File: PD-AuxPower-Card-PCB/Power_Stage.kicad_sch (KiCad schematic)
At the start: 33 parts, among them J4 2.54mm terminal, Q1 FDMC86520L, T1 EFD10, U8 EL3H7(C)(TA)-G, U9 TL431DBZ

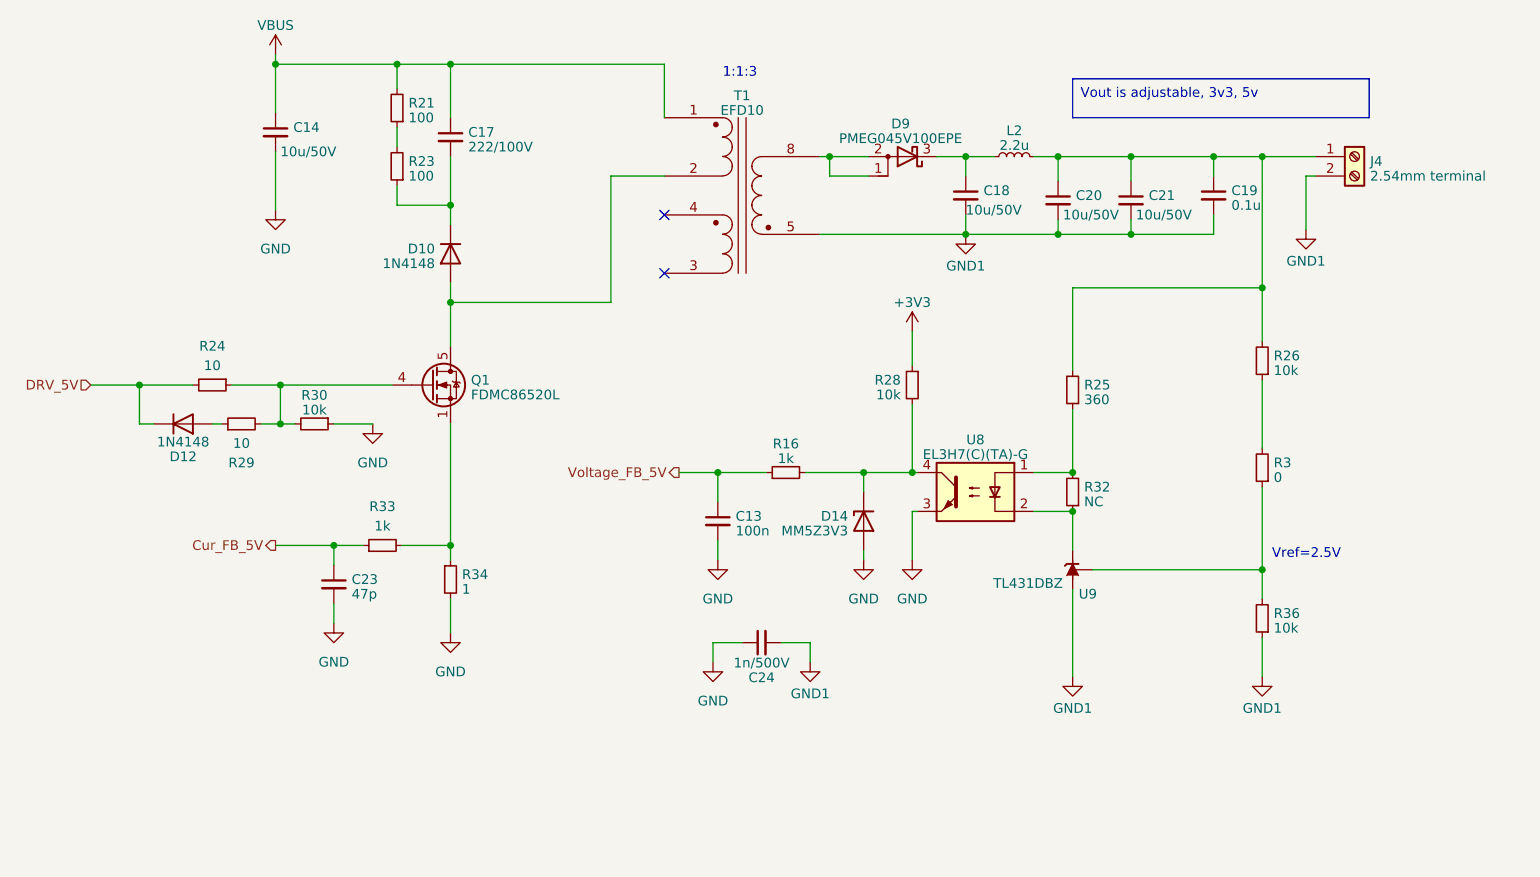
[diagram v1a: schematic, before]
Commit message: FEAT: Change PWM frequency to 50kHz, fix LED indicator bug PCB FIX: Adjust ophotocoupler feedback resistor value
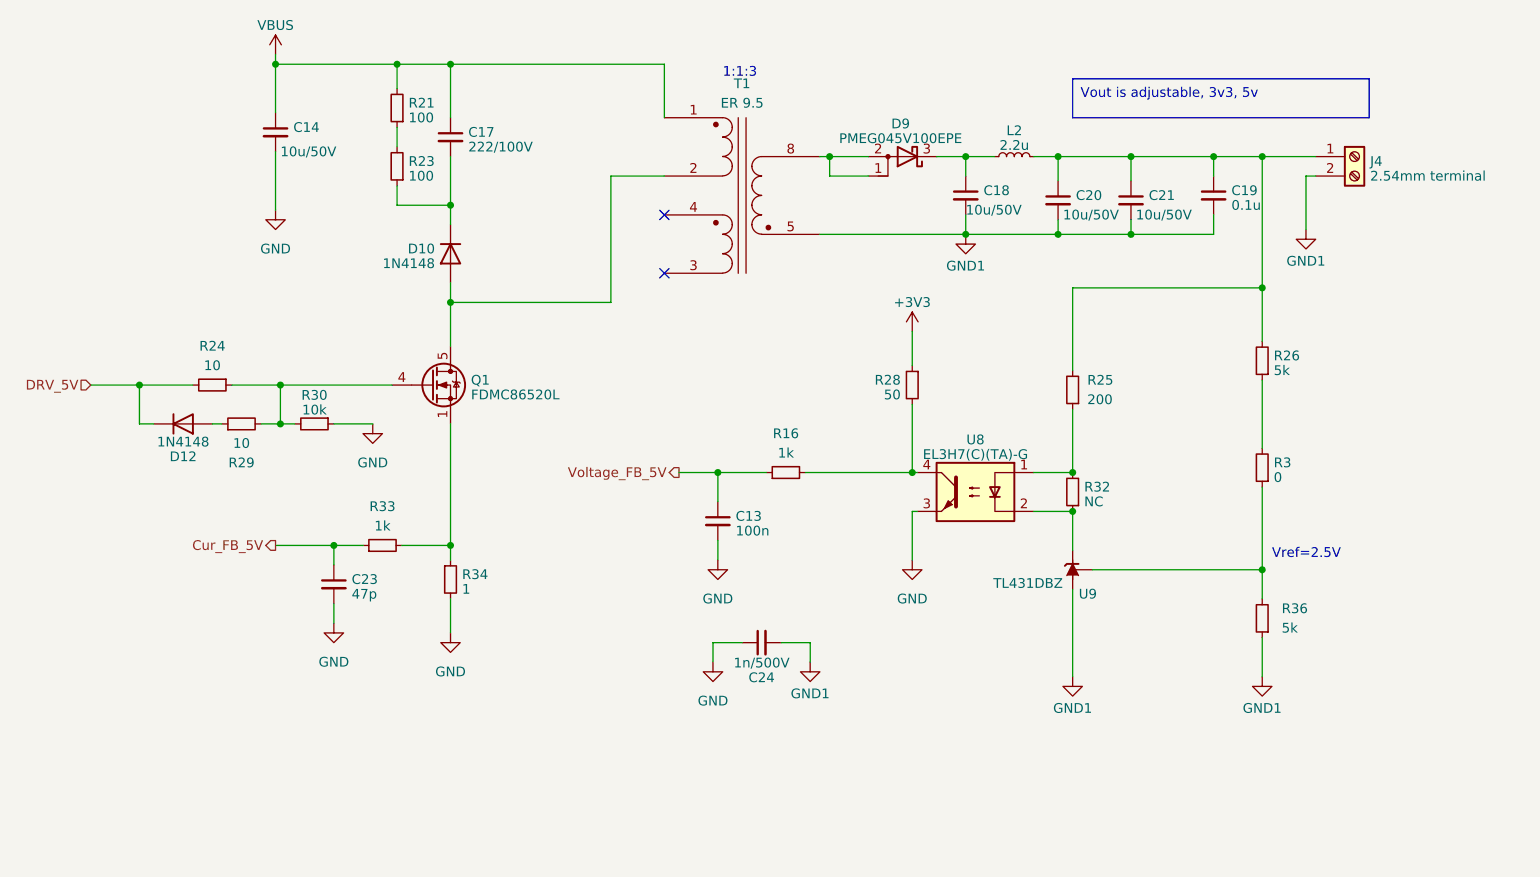
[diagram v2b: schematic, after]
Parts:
- removed D14: MM5Z3V3, Diode_SMD:D_SOD-523, symbol Diode:BZV55B3V3
- R25: value 360 -> 200
- R26, R36: value 10k -> 5k
- R28: value 10k -> 50
- T1: value EFD10 -> ER 9.5
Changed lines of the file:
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@@
   (junction (at 111.125 86.995) (diameter 0) (color 0 0 0 0)
-  )
-  (junction (at 165.1 109.22) (diameter 0) (color 0 0 0 0)
   )
   (junction (at 190.5 67.945) (diameter 0) (color 0 0 0 0)
@@
     (stroke (width 0) (type default))
   )
-  (wire (pts (xy 165.1 119.38) (xy 165.1 120.65))
-    (stroke (width 0) (type default))
-  )
   (wire (pts (xy 192.405 124.46) (xy 192.405 135.89))
     (stroke (width 0) (type default))
@@
     (stroke (width 0) (type default))
   )
-  (wire (pts (xy 165.1 109.22) (xy 171.45 109.22))
+  (wire (pts (xy 157.48 109.22) (xy 171.45 109.22))
     (stroke (width 0) (type default))
   )
@@
     (stroke (width 0) (type default))
   )
-  (wire (pts (xy 165.1 111.76) (xy 165.1 109.22))
-    (stroke (width 0) (type default))
-  )
   (wire (pts (xy 64.135 97.79) (xy 70.485 97.79))
     (stroke (width 0) (type default))
@@
   )
   (wire (pts (xy 160.655 67.945) (xy 165.735 67.945))
-    (stroke (width 0) (type default))
-  )
-  (wire (pts (xy 157.48 109.22) (xy 165.1 109.22))
     (stroke (width 0) (type default))
   )
@@
   (symbol (lib_id "Device:R_Small") (at 192.405 98.425 180) (unit 1)
     (in_bom yes) (on_board yes) (dnp no) (fields_autoplaced)
-    (property "Reference" "R25" (at 193.9036 97.7813 0)
-      (effects (font (size 1.27 1.27)) (justify right))
-    )
-    (property "Value" "360" (at 193.9036 99.7023 0)
+    (property "Reference" "R25" (at 194.31 97.155 0)
+      (effects (font (size 1.27 1.27)) (justify right))
+    )
+    (property "Value" "200" (at 194.31 99.695 0)
       (effects (font (size 1.27 1.27)) (justify right))
     )
@@
   (symbol (lib_id "Device:R_Small") (at 154.94 109.22 90) (unit 1)
     (in_bom yes) (on_board yes) (dnp no) (fields_autoplaced)
-    (property "Reference" "R16" (at 154.94 105.4735 90)
-      (effects (font (size 1.27 1.27)))
-    )
-    (property "Value" "1k" (at 154.94 107.3945 90)
+    (property "Reference" "R16" (at 154.94 104.14 90)
+      (effects (font (size 1.27 1.27)))
+    )
+    (property "Value" "1k" (at 154.94 106.68 90)
       (effects (font (size 1.27 1.27)))
     )
@@
       (effects (font (size 1.27 1.27)) (justify left))
     )
-    (property "Value" "10k" (at 169.9514 99.0673 0)
+    (property "Value" "50" (at 169.9514 99.0673 0)
       (effects (font (size 1.27 1.27)) (justify left))
     )
@@
         (path "/48c5bc14-ccc3-44de-b526-838e3d53c0ee/40f113c1-6183-4863-b2ec-a4ca33698158"
           (reference "#PWR055") (unit 1)
-        )
-      )
-    )
-  )
-  (symbol (lib_id "power:GND") (at 165.1 120.65 0) (unit 1)
-    (in_bom yes) (on_board yes) (dnp no) (fields_autoplaced)
-    (property "Reference" "#PWR08" (at 165.1 127 0)
-      (effects (font (size 1.27 1.27)) hide)
-    )
-    (property "Value" "GND" (at 165.1 125.73 0)
-      (effects (font (size 1.27 1.27)))
-    )
-    (property "Footprint" "" (at 165.1 120.65 0)
-      (effects (font (size 1.27 1.27)) hide)
-    )
-    (property "Datasheet" "" (at 165.1 120.65 0)
-      (effects (font (size 1.27 1.27)) hide)
-    )
-    (pin "1")
-    (instances
-      (project "PD-AuxPower-Card"
-        (path "/48c5bc14-ccc3-44de-b526-838e3d53c0ee"
-          (reference "#PWR08") (unit 1)
-        )
-        (path "/48c5bc14-ccc3-44de-b526-838e3d53c0ee/40f113c1-6183-4863-b2ec-a4ca33698158"
-          (reference "#PWR064") (unit 1)
         )
       )
@@
     )
   )
-  (symbol (lib_id "Diode:BZV55B3V3") (at 165.1 115.57 90) (mirror x) (unit 1)
-    (in_bom yes) (on_board yes) (dnp no)
-    (property "Reference" "D14" (at 163.068 114.9263 90)
-      (effects (font (size 1.27 1.27)) (justify left))
-    )
-    (property "Value" "MM5Z3V3" (at 163.068 116.8473 90)
-      (effects (font (size 1.27 1.27)) (justify left))
-    )
-    (property "Footprint" "Diode_SMD:D_SOD-523" (at 169.545 115.57 0)
-      (effects (font (size 1.27 1.27)) hide)
-    )
-    (property "Datasheet" "https://assets.nexperia.com/documents/data-sheet/BZV55_SER.pdf" (at 165.1 115.57 0)
-      (effects (font (size 1.27 1.27)) hide)
-    )
-    (pin "1")
-    (pin "2")
-    (instances
-      (project "PD-AuxPower-Card"
-        (path "/48c5bc14-ccc3-44de-b526-838e3d53c0ee/40f113c1-6183-4863-b2ec-a4ca33698158"
-          (reference "D14") (unit 1)
-        )
-      )
-    )
-  )
   (symbol (lib_id "Device:R_Small") (at 217.17 94.615 180) (unit 1)
     (in_bom yes) (on_board yes) (dnp no)
@@
       (effects (font (size 1.27 1.27)) (justify right))
     )
-    (property "Value" "10k" (at 218.6686 95.8923 0)
+    (property "Value" "5k" (at 218.6686 95.8923 0)
       (effects (font (size 1.27 1.27)) (justify right))
     )
@@
   (symbol (lib_id "Device:Transformer_1P_2S") (at 149.225 73.025 0) (mirror y) (unit 1)
     (in_bom yes) (on_board yes) (dnp no) (fields_autoplaced)
-    (property "Reference" "T1" (at 149.225 59.9819 0)
-      (effects (font (size 1.27 1.27)))
-    )
-    (property "Value" "EFD10" (at 149.225 61.9029 0)
+    (property "Reference" "T1" (at 149.225 58.42 0)
+      (effects (font (size 1.27 1.27)))
+    )
+    (property "Value" "ER 9.5" (at 149.225 60.96 0)
       (effects (font (size 1.27 1.27)))
     )
@@
   (symbol (lib_id "Device:R_Small") (at 217.17 128.27 180) (unit 1)
     (in_bom yes) (on_board yes) (dnp no) (fields_autoplaced)
-    (property "Reference" "R36" (at 218.6686 127.6263 0)
-      (effects (font (size 1.27 1.27)) (justify right))
-    )
-    (property "Value" "10k" (at 218.6686 129.5473 0)
-      (effects (font (size 1.27 1.27)) (justify right))
-    )
+    (property "Reference" "R36" (at 219.71 127 0)
+      (effects (font (size 1.27 1.27)) (justify right))
+    )
+    (property "Value" "5k" (at 219.71 129.54 0)
+      (effects (font (size 1.27 1.27)) (justify right))
+    )

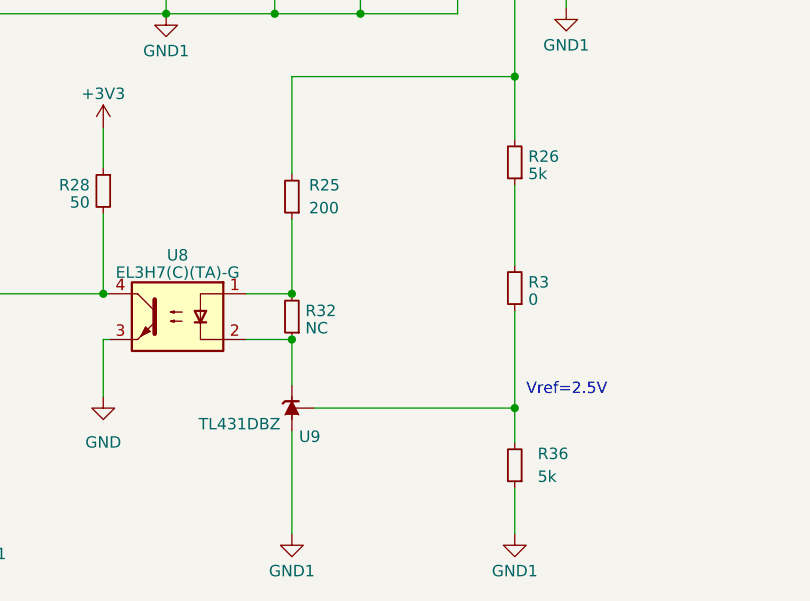
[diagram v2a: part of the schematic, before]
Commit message: FEAT: Add PID algorithm for output voltage control. NOT TUNE YET! Change ADC1 trigger source into TIM1 TRGO for update event. Synchronised TIM2 and TIM1 by using slave mode. PCB: Change TL431 to TLV431 for 3.3V output rail. Change some tuned resistor value for next sample.
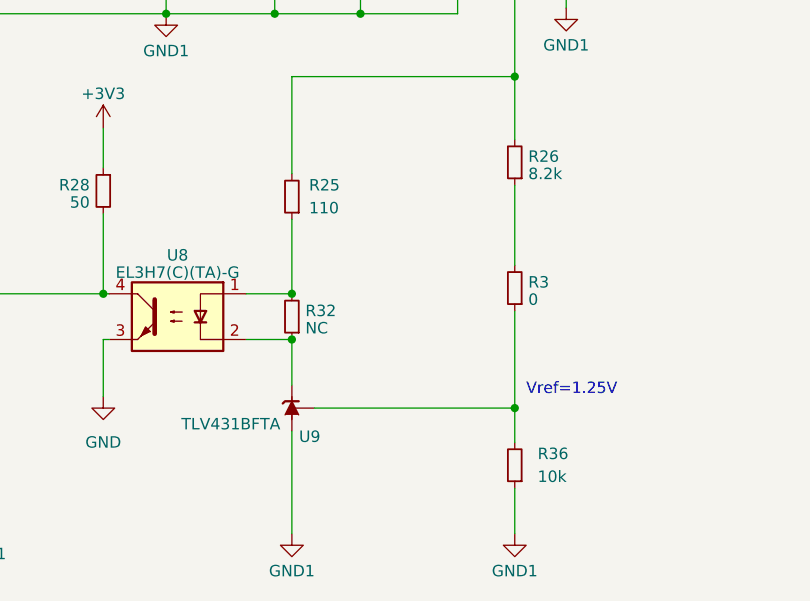
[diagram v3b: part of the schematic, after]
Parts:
- R25: value 200 -> 110
- R26: value 5k -> 8.2k
- R36: value 5k -> 10k
- U9: value TL431DBZ -> TLV431BFTA
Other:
- note added: "Vref=1.25V"
- note removed: "Vref=2.5V"
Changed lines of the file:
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@@
     (effects (font (size 1.27 1.27)) (justify left top))
   )
-  (text "Vref=2.5V" (at 218.44 120.65 0)
+  (text "Vref=1.25V" (at 218.44 120.65 0)
     (effects (font (size 1.27 1.27)) (justify left bottom))
   )
@@
       (effects (font (size 1.27 1.27)) (justify right))
     )
-    (property "Value" "200" (at 194.31 99.695 0)
+    (property "Value" "110" (at 194.31 99.695 0)
       (effects (font (size 1.27 1.27)) (justify right))
     )
@@
       (effects (font (size 1.27 1.27)) (justify right))
     )
-    (property "Value" "5k" (at 218.6686 95.8923 0)
+    (property "Value" "8.2k" (at 218.6686 95.8923 0)
       (effects (font (size 1.27 1.27)) (justify right))
     )
@@
       (effects (font (size 1.27 1.27)) (justify right))
     )
-    (property "Value" "TL431DBZ" (at 191.1277 123.698 90)
+    (property "Value" "TLV431BFTA" (at 191.1277 123.698 90)
       (effects (font (size 1.27 1.27)) (justify right))
     )
@@
       (effects (font (size 1.27 1.27)) (justify right))
     )
-    (property "Value" "5k" (at 219.71 129.54 0)
-      (effects (font (size 1.27 1.27)) (justify right))
-    )
+    (property "Value" "10k" (at 219.71 129.54 0)
+      (effects (font (size 1.27 1.27)) (justify right))
+    )

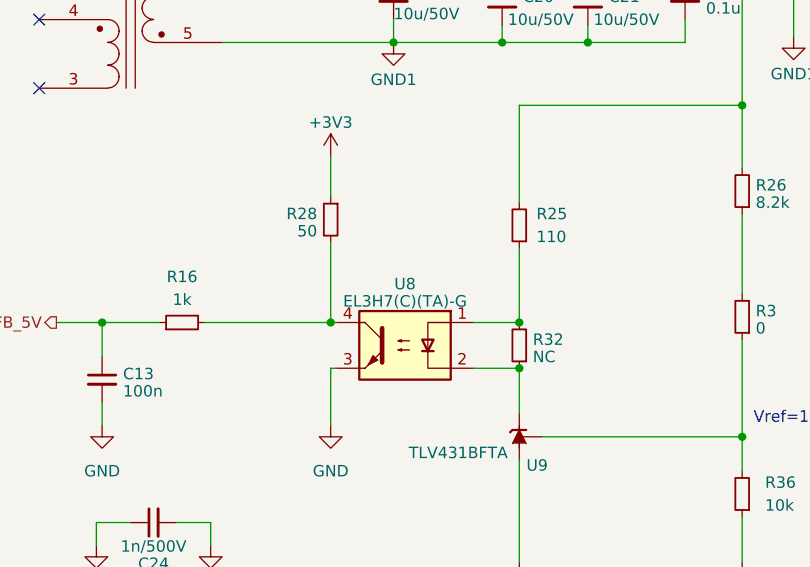
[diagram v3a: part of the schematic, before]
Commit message: PCB: Update LTV-214 footprint and update to PCB layout.
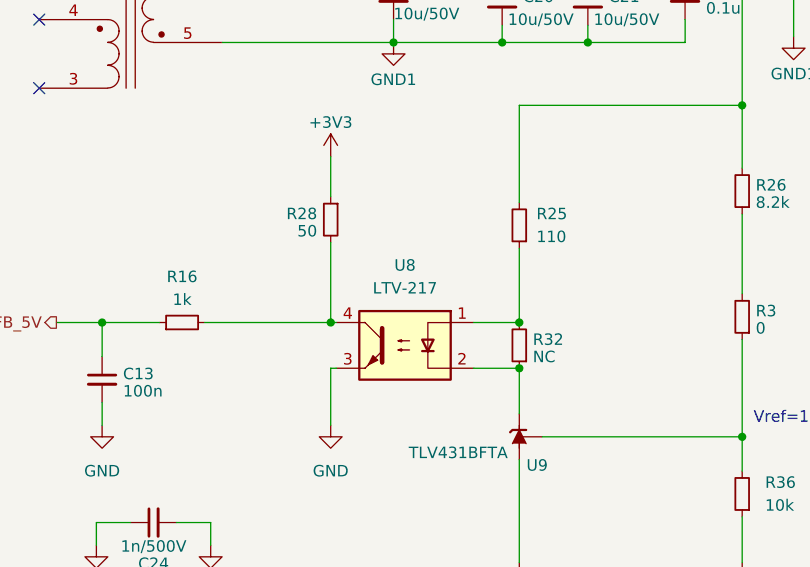
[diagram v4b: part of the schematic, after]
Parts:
- U8: value EL3H7(C)(TA)-G -> LTV-217; footprint OptoDevice:Panasonic_APV-AQY_SSOP-4_4.45x2.65mm_P1.27mm -> Library:SOP-4-175mil
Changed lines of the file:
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@@
   (symbol (lib_id "Isolator:LTV-817") (at 179.705 111.76 0) (mirror y) (unit 1)
     (in_bom yes) (on_board yes) (dnp no) (fields_autoplaced)
-    (property "Reference" "U8" (at 179.705 104.9401 0)
+    (property "Reference" "U8" (at 179.705 102.87 0)
       (effects (font (size 1.27 1.27)))
     )
-    (property "Value" "EL3H7(C)(TA)-G" (at 179.705 106.8611 0)
+    (property "Value" "LTV-217" (at 179.705 105.41 0)
       (effects (font (size 1.27 1.27)))
     )
-    (property "Footprint" "OptoDevice:Panasonic_APV-AQY_SSOP-4_4.45x2.65mm_P1.27mm" (at 184.785 116.84 0)
+    (property "Footprint" "Library:SOP-4-175mil" (at 184.785 116.84 0)
       (effects (font (size 1.27 1.27) italic) (justify left) hide)
     )

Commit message: FEAT: Set I2C mode to standard mode(100kHz), change FUSB302B driver header file definition, trimming output voltage of 3.3/5V channel and 12/24V channel by optocoupler current reduce to 1mA. Add reserved PD protocol header and source file named pd_sink.h/.c. Add FUSB302B initial sequence and read/write driver. PCB: remove some unused protection diode, modify resistance.
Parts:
- removed R29: 10, Resistor_SMD:R_0402_1005Metric, symbol Device:R_Small
- R25: value 110 -> 1k
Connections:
- net at Q1.4 (G), R24.1, R30.2: now also D12.2 (A)
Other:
- moved on the sheet: D12
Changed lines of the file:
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@@
-    (stroke (width 0) (type default))
-  )
-  (wire (pts (xy 80.01 102.87) (xy 81.28 102.87))
     (stroke (width 0) (type default))
   )
@@
     (stroke (width 0) (type default))
   )
-  (wire (pts (xy 70.485 102.87) (xy 72.39 102.87))
+  (wire (pts (xy 70.485 102.87) (xy 75.565 102.87))
     (stroke (width 0) (type default))
   )
@@
     (stroke (width 0) (type default))
   )
-  (wire (pts (xy 86.36 102.87) (xy 88.9 102.87))
+  (wire (pts (xy 83.185 102.87) (xy 88.9 102.87))
     (stroke (width 0) (type default))
   )
@@
       (effects (font (size 1.27 1.27)) (justify right))
     )
-    (property "Value" "110" (at 194.31 99.695 0)
+    (property "Value" "1k" (at 194.31 99.695 0)
       (effects (font (size 1.27 1.27)) (justify right))
     )
@@
     )
   )
-  (symbol (lib_id "Diode:1N4148") (at 76.2 102.87 0) (mirror x) (unit 1)
-    (in_bom yes) (on_board yes) (dnp no)
-    (property "Reference" "D12" (at 76.2 107.1499 0)
-      (effects (font (size 1.27 1.27)))
-    )
-    (property "Value" "1N4148" (at 76.2 105.2289 0)
-      (effects (font (size 1.27 1.27)))
-    )
-    (property "Footprint" "Diode_SMD:D_SOD-523" (at 76.2 102.87 0)
-      (effects (font (size 1.27 1.27)) hide)
-    )
-    (property "Datasheet" "https://assets.nexperia.com/documents/data-sheet/1N4148_1N4448.pdf" (at 76.2 102.87 0)
-      (effects (font (size 1.27 1.27)) hide)
-    )
-    (property "Sim.Device" "D" (at 76.2 102.87 0)
-      (effects (font (size 1.27 1.27)) hide)
-    )
-    (property "Sim.Pins" "1=K 2=A" (at 76.2 102.87 0)
+  (symbol (lib_id "Diode:1N4148") (at 79.375 102.87 0) (mirror x) (unit 1)
+    (in_bom yes) (on_board yes) (dnp no)
+    (property "Reference" "D12" (at 79.375 107.1499 0)
+      (effects (font (size 1.27 1.27)))
+    )
+    (property "Value" "1N4148" (at 79.375 105.2289 0)
+      (effects (font (size 1.27 1.27)))
+    )
+    (property "Footprint" "Diode_SMD:D_SOD-523" (at 79.375 102.87 0)
+      (effects (font (size 1.27 1.27)) hide)
+    )
+    (property "Datasheet" "https://assets.nexperia.com/documents/data-sheet/1N4148_1N4448.pdf" (at 79.375 102.87 0)
+      (effects (font (size 1.27 1.27)) hide)
+    )
+    (property "Sim.Device" "D" (at 79.375 102.87 0)
+      (effects (font (size 1.27 1.27)) hide)
+    )
+    (property "Sim.Pins" "1=K 2=A" (at 79.375 102.87 0)
       (effects (font (size 1.27 1.27)) hide)
     )
@@
         )
       )
-    )
-  )
-  (symbol (lib_id "Device:R_Small") (at 83.82 102.87 90) (unit 1)
-    (in_bom yes) (on_board yes) (dnp no)
-    (property "Reference" "R29" (at 83.82 107.95 90)
-      (effects (font (size 1.27 1.27)))
-    )
-    (property "Value" "10" (at 83.82 105.41 90)
-      (effects (font (size 1.27 1.27)))
-    )
-    (property "Footprint" "Resistor_SMD:R_0402_1005Metric" (at 83.82 102.87 0)
-      (effects (font (size 1.27 1.27)) hide)
-    )
-    (property "Datasheet" "~" (at 83.82 102.87 0)
-      (effects (font (size 1.27 1.27)) hide)
-    )
-    (pin "1")
-    (pin "2")
-    (instances
-      (project "PD-AuxPower-Card"
-        (path "/48c5bc14-ccc3-44de-b526-838e3d53c0ee/40f113c1-6183-4863-b2ec-a4ca33698158"
-          (reference "R29") (unit 1)
-        )
-      )
